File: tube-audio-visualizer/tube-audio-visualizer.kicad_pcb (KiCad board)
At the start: 2 copper layers, 24 parts, among them J1 AudioJack3_SwitchTR, J2 Barrel_Jack_Switch, T1 EM80, U1 NCH6100HV, U2 LM741, U3 LM386

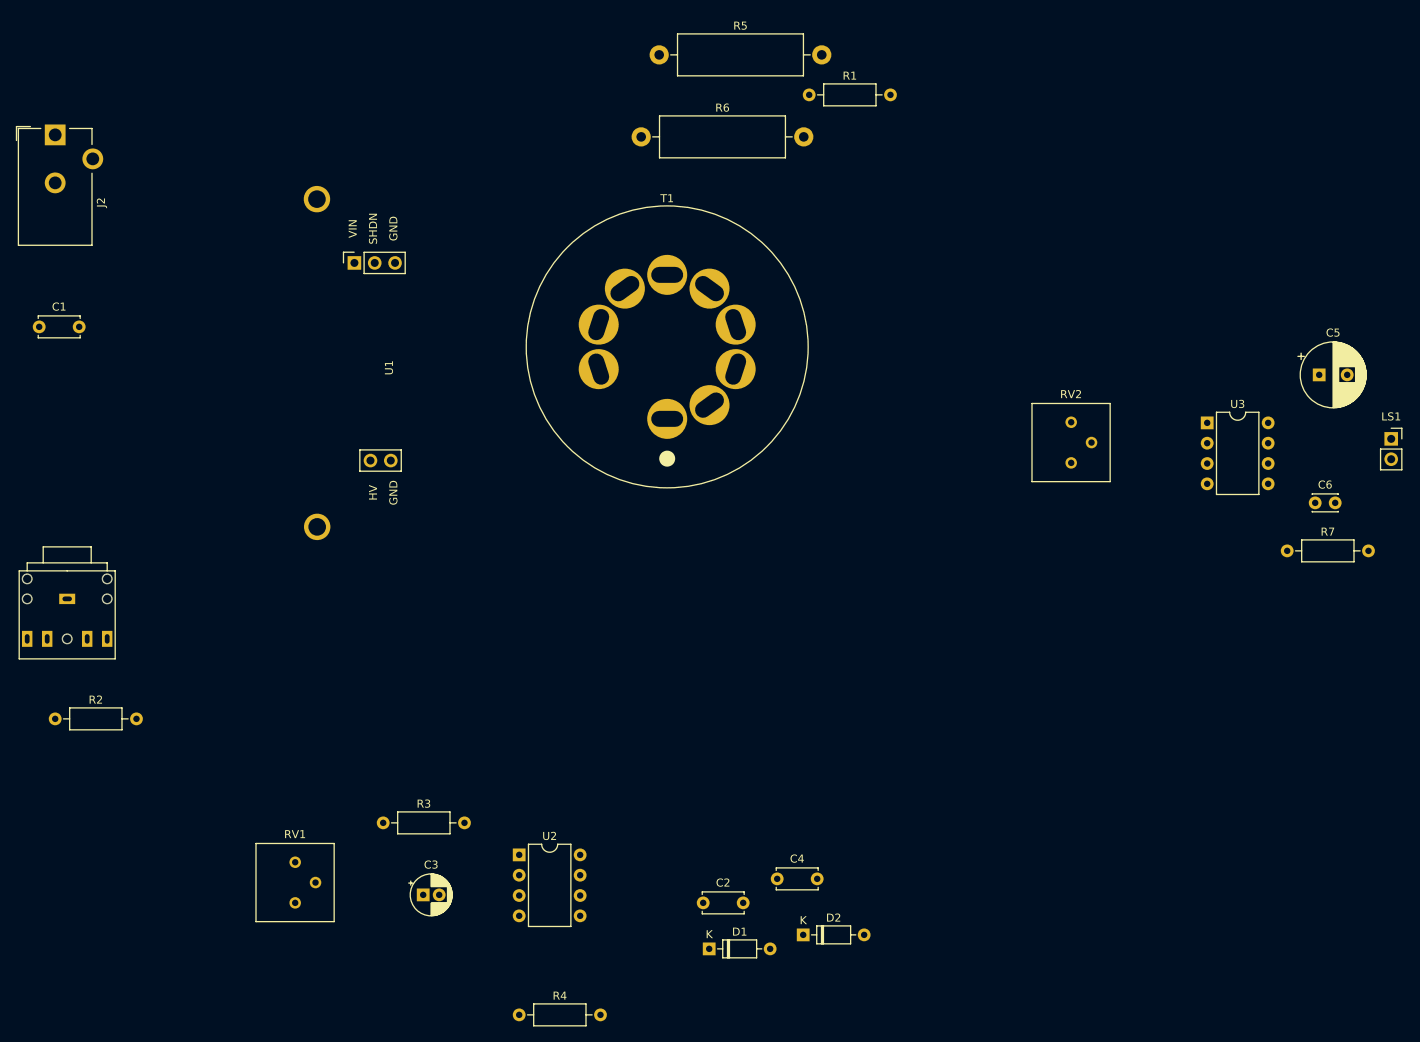
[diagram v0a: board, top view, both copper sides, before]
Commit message: Parts and tracks laid. Adding text and extra silkscreen layer before sending off.
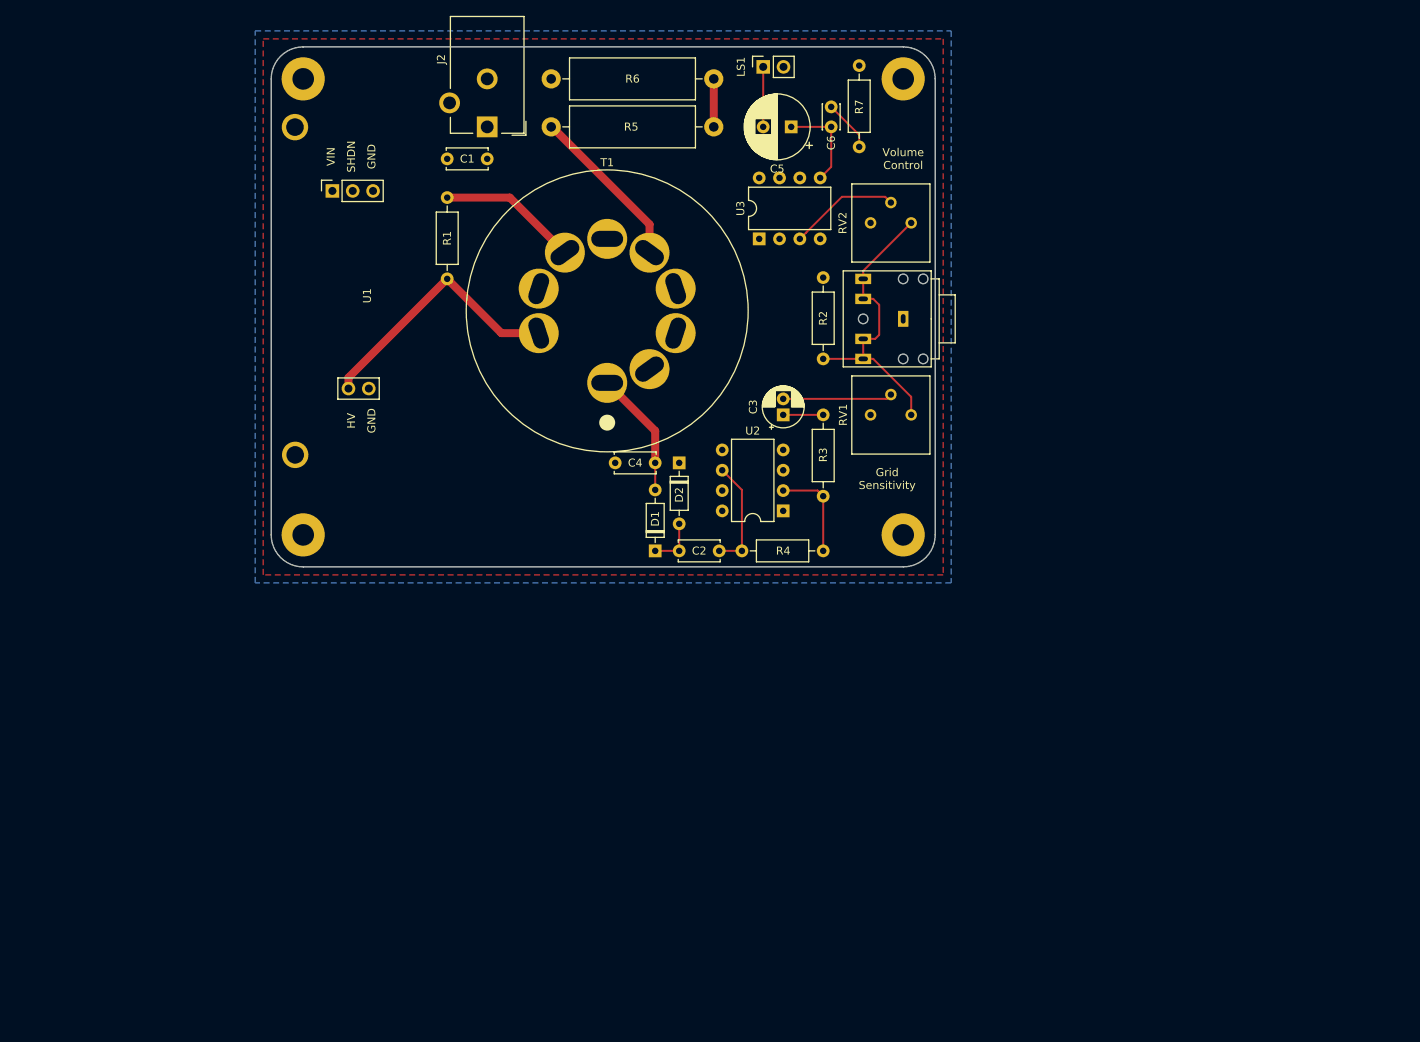
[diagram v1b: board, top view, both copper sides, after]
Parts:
- added REF**: MountingHole_2.7mm_M2.5_Pad, MountingHole:MountingHole_2.7mm_M2.5_Pad, F.Cu at (179.0, 101.0)
- added REF**: MountingHole_2.7mm_M2.5_Pad, MountingHole:MountingHole_2.7mm_M2.5_Pad, F.Cu at (104.0, 101.0)
- added REF**: MountingHole_2.7mm_M2.5_Pad, MountingHole:MountingHole_2.7mm_M2.5_Pad, F.Cu at (104.0, 44.0)
- added REF**: MountingHole_2.7mm_M2.5_Pad, MountingHole:MountingHole_2.7mm_M2.5_Pad, F.Cu at (179.0, 44.0)
- moved J1 110.2 mm to (179.0, 74.0), turned to 270 degrees
- moved R2 106.0 mm to (169.0, 79.0), turned to 90 degrees
- moved RV1 98.2 mm to (180.0, 86.0), turned to 90 degrees
- moved LS1 91.2 mm to (161.5, 42.5), turned to 90 degrees
- moved C6 76.6 mm to (170.0, 50.0), turned to 90 degrees
- moved C3 75.0 mm to (164.0, 86.0), turned to 90 degrees
- moved R7 73.6 mm to (173.5, 52.5), turned to 90 degrees
- moved C5 72.9 mm to (165.0, 50.0), turned to 180 degrees
- moved R3 68.5 mm to (169.0, 96.2), turned to 90 degrees
- moved R4 64.3 mm to (158.8, 103.0)
- moved D2 61.0 mm to (151.0, 92.0), turned to 270 degrees
- moved U3 60.5 mm to (161.0, 64.0), turned to 90 degrees
- moved C1 59.8 mm to (127.0, 54.0), turned to 180 degrees
- moved U2 54.2 mm to (164.0, 98.0), turned to 180 degrees
- moved C4 54.2 mm to (148.0, 92.0), turned to 180 degrees
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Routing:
- net AC: track 0.00 -> 38.0 mm
- net +180V: track 0.00 -> 33.1 mm
- net Net-(R5-Pad2): track 0.00 -> 20.9 mm
- net Net-(R1-Pad2): track 0.00 -> 17.6 mm
- net Net-(C4-Pad1): track 0.00 -> 15.9 mm
- net /741out: track 0.00 -> 13.9 mm
- net Net-(RV2-Pad2): track 0.00 -> 13.9 mm
- net Net-(C3-Pad2): track 0.00 -> 13.7 mm
- net Net-(R3-Pad1): track 0.00 -> 12.1 mm
- net /386out: track 0.00 -> 12.0 mm
- net Net-(C5-Pad2): track 0.00 -> 7.50 mm
- net Net-(C6-Pad2): track 0.00 -> 6.45 mm
- net Net-(C2-Pad1): track 0.00 -> 6.38 mm
- net Net-(R5-Pad1): track 0.00 -> 6.00 mm
- net Net-(C3-Pad1): track 0.00 -> 5.00 mm
- added copper zone on F.Cu, net +12V
- added copper zone on B.Cu, net GND
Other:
- board outline added: 83 x 65 mm
- board text added: "Grid Sensitivity"
- board text added: "Volume Control"

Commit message: Tube audio visualizer ready to be sent to fab. Added hot surface warning symbol footprint.
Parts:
- added C7: 1uF, footprints-nad:Cap_Film_250V_1uF_Nichicon, F.Cu at (122.0, 82.0)
- added G***: LOGO, footprints-nad:pikachu1, F.Cu at (111.0, 97.0)
- added G***: LOGO, footprints-nad:hot-surface-warning, F.Cu at (155.2, 54.2)
- added REF**: Symbol_HighVoltage_Type2_CopperTop_VerySmall, Symbol:Symbol_HighVoltage_Type2_CopperTop_VerySmall, F.Cu at (134.0, 95.0)
- moved C4 0.50 mm to (148.0, 92.5)
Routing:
- net +180V: track 33.1 -> 46.1 mm
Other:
- board text added: "+"
- board text added: "HIGH VOLTAGE"
- board text added: "HOT"
- board text added: "M2.5"
- board text added: "Nathan Aquino Dornback September 12, 2020 To Ella, Frank, Dean, and Louis, without whose company creating these boards would be less enjoyable."
